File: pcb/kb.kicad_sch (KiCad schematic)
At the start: 72 parts, among them K1 Gateron_LP_2.0, K10 Gateron_LP_2.0, K11 Gateron_LP_2.0, K12 Gateron_LP_2.0, K13 Gateron_LP_2.0, K14 Gateron_LP_2.0, K15 Gateron_LP_2.0, K16 Gateron_LP_2.0, K17 Gateron_LP_2.0, K18 Gateron_LP_2.0, K19 Gateron_LP_2.0, K2 Gateron_LP_2.0, K20 Gateron_LP_2.0, K21 Gateron_LP_2.0, K22 Gateron_LP_2.0, K23 Gateron_LP_2.0, K24 Gateron_LP_2.0, K25 Gateron_LP_2.0, K26 Gateron_LP_2.0, K27 Gateron_LP_2.0, K28 Gateron_LP_2.0, K29 Gateron_LP_2.0, K3 Gateron_LP_2.0, K30 Gateron_LP_2.0, K31 Gateron_LP_2.0, K32 Gateron_LP_2.0, K33 Gateron_LP_2.0, K34 Gateron_LP_2.0, K35 Gateron_LP_2.0, K36 Gateron_LP_2.0, K37 Gateron_LP_2.0, K38 Gateron_LP_2.0, K39 Gateron_LP_2.0, K4 Gateron_LP_2.0, K40 Gateron_LP_2.0, K41 Gateron_LP_2.0, K42 Gateron_LP_2.0, K43 Gateron_LP_2.0, K44 Gateron_LP_2.0, K45 Gateron_LP_2.0, K46 Gateron_LP_2.0, K47 Gateron_LP_2.0, K48 Gateron_LP_2.0, K49 Gateron_LP_2.0, K5 Gateron_LP_2.0, K50 Gateron_LP_2.0, K51 Gateron_LP_2.0, K52 Gateron_LP_2.0, K53 Gateron_LP_2.0, K54 Gateron_LP_2.0, K55 Gateron_LP_2.0, K56 Gateron_LP_2.0, K57 Gateron_LP_2.0, K58 Gateron_LP_2.0, K59 Gateron_LP_2.0, K6 Gateron_LP_2.0, K60 Gateron_LP_2.0, K61 Gateron_LP_2.0, K62 Gateron_LP_2.0, K63 Gateron_LP_2.0, K64 Gateron_LP_2.0, K7 Gateron_LP_2.0, K8 Gateron_LP_2.0, K9 Gateron_LP_2.0, U1 SuperMini nRF52840

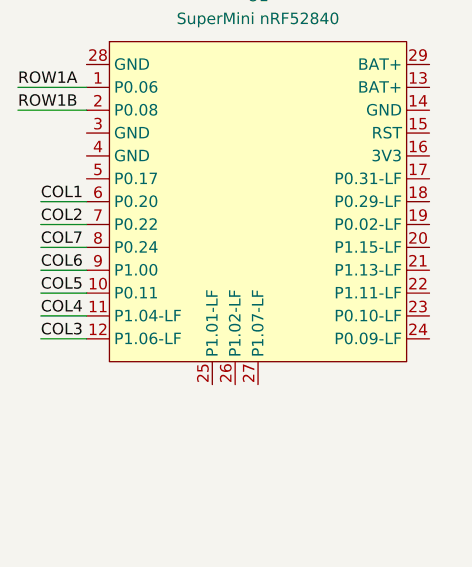
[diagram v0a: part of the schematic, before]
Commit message: routed column traces
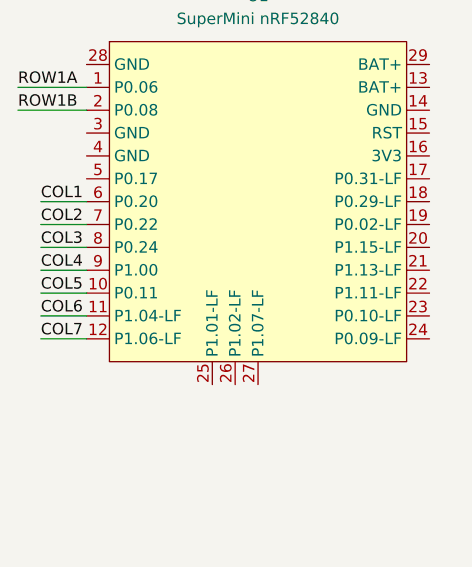
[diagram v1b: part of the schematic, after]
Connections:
- net COL3: now also U1.8 (P0.24); no longer U1.12 (P1.06-LF)
- net COL4: now also U1.9 (P1.00); no longer U1.11 (P1.04-LF)
- net COL6: now also U1.11 (P1.04-LF); no longer U1.9 (P1.00)
- net COL7: now also U1.12 (P1.06-LF); no longer U1.8 (P0.24)

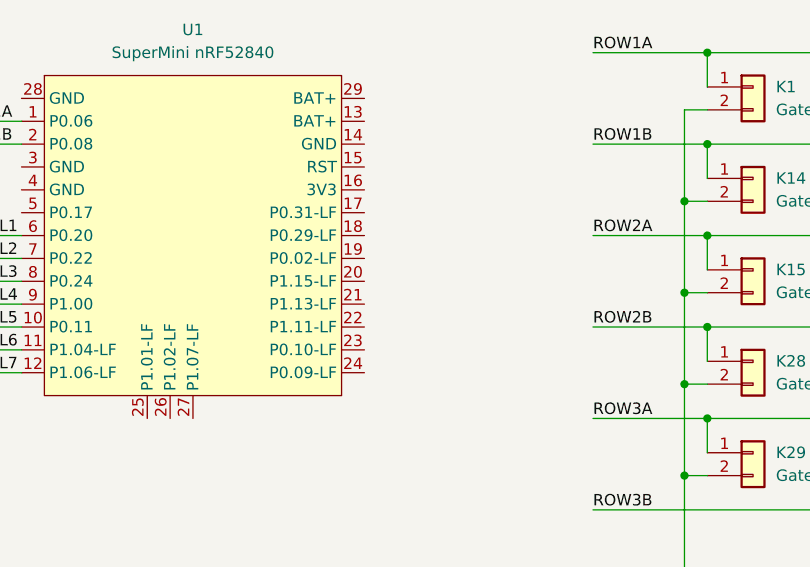
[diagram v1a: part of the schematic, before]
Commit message: routed all traces
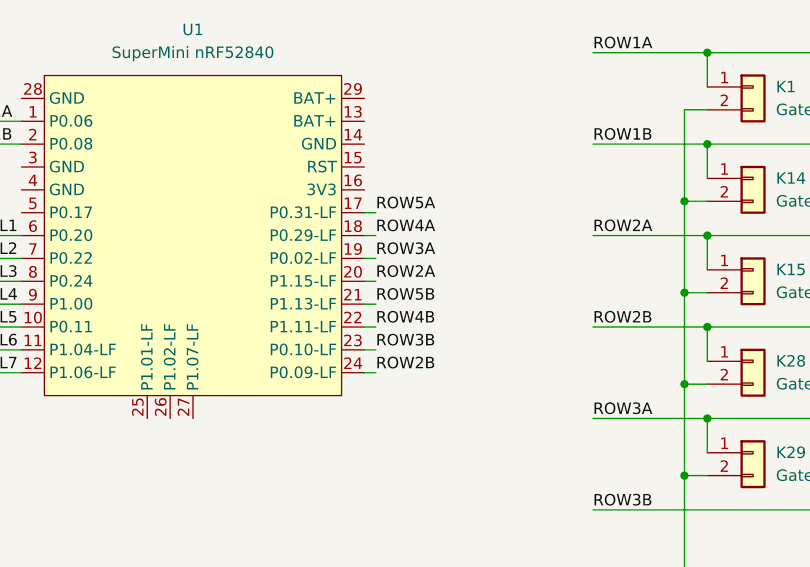
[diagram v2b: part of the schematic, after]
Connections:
- net ROW2A: now also U1.20 (P1.15-LF)
- net ROW2B: now also U1.24 (P0.09-LF)
- net ROW3A: now also U1.19 (P0.02-LF)
- net ROW3B: now also U1.23 (P0.10-LF)
- net ROW4A: now also U1.18 (P0.29-LF)
- net ROW4B: now also U1.22 (P1.11-LF)
- net ROW5A: now also U1.17 (P0.31-LF)
- net ROW5B: now also U1.21 (P1.13-LF)
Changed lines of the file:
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@@
+	(wire
+		(pts
+			(xy 63.5 57.15) (xy 64.77 57.15)
+		)
+		(stroke
+			(width 0)
+			(type default)
+		)
+	)
 	(wire
 		(pts
@@
 	(wire
 		(pts
+			(xy 63.5 44.45) (xy 64.77 44.45)
+		)
+		(stroke
+			(width 0)
+			(type default)
+		)
+	)
+	(wire
+		(pts
 			(xy 175.26 68.58) (xy 177.8 68.58)
 		)
@@
 	(wire
 		(pts
+			(xy 63.5 49.53) (xy 64.77 49.53)
+		)
+		(stroke
+			(width 0)
+			(type default)
+		)
+	)
+	(wire
+		(pts
 			(xy 20.32 41.91) (xy 25.4 41.91)
 		)
@@
 	(wire
 		(pts
+			(xy 63.5 39.37) (xy 64.77 39.37)
+		)
+		(stroke
+			(width 0)
+			(type default)
+		)
+	)
+	(wire
+		(pts
 			(xy 228.6 82.55) (xy 254 82.55)
 		)
@@
 	(wire
 		(pts
+			(xy 63.5 46.99) (xy 64.77 46.99)
+		)
+		(stroke
+			(width 0)
+			(type default)
+		)
+	)
+	(wire
+		(pts
 			(xy 152.4 82.55) (xy 152.4 86.36)
 		)
@@
 	(wire
 		(pts
+			(xy 63.5 54.61) (xy 64.77 54.61)
+		)
+		(stroke
+			(width 0)
+			(type default)
+		)
+	)
+	(wire
+		(pts
 			(xy 152.4 21.59) (xy 152.4 25.4)
 		)
@@
 	(wire
 		(pts
+			(xy 63.5 41.91) (xy 64.77 41.91)
+		)
+		(stroke
+			(width 0)
+			(type default)
+		)
+	)
+	(wire
+		(pts
 			(xy 149.86 88.9) (xy 149.86 99.06)
 		)
@@
 		(pts
 			(xy 200.66 78.74) (xy 203.2 78.74)
+		)
+		(stroke
+			(width 0)
+			(type default)
+		)
+	)
+	(wire
+		(pts
+			(xy 63.5 52.07) (xy 64.77 52.07)
 		)
 		(stroke
@@
 		)
 	)
+	(label "ROW4A"
+		(at 64.77 41.91 0)
+		(effects
+			(font
+				(size 1.27 1.27)
+			)
+			(justify left bottom)
+		)
+	)
+	(label "ROW2A"
+		(at 64.77 46.99 0)
+		(effects
+			(font
+				(size 1.27 1.27)
+			)
+			(justify left bottom)
+		)
+	)
 	(label "COL5"
 		(at 20.32 52.07 0)
@@
 		)
 	)
+	(label "ROW5A"
+		(at 64.77 39.37 0)
+		(effects
+			(font
+				(size 1.27 1.27)
+			)
+			(justify left bottom)
+		)
+	)
 	(label "COL7"
 		(at 251.46 139.7 0)
@@
 		)
 	)
+	(label "ROW4B"
+		(at 64.77 52.07 0)
+		(effects
+			(font
+				(size 1.27 1.27)
+			)
+			(justify left bottom)
+		)
+	)
 	(label "COL2"
 		(at 20.32 44.45 0)
@@
 		)
 	)
+	(label "ROW5B"
+		(at 64.77 49.53 0)
+		(effects
+			(font
+				(size 1.27 1.27)
+			)
+			(justify left bottom)
+		)
+	)
 	(label "COL3"
 		(at 20.32 46.99 0)
@@
 		)
 	)
+	(label "ROW3A"
+		(at 64.77 44.45 0)
+		(effects
+			(font
+				(size 1.27 1.27)
+			)
+			(justify left bottom)
+		)
+	)
 	(label "ROW2A"
 		(at 88.9 41.91 0)
@@
 		)
 	)
+	(label "ROW2B"
+		(at 64.77 57.15 0)
+		(effects
+			(font
+				(size 1.27 1.27)
+			)
+			(justify left bottom)
+		)
+	)
 	(label "COL4"
 		(at 20.32 49.53 0)
@@
 		(effects
 			(font
+				(size 1.27 1.27)
+			)
+			(justify left bottom)
+		)
+	)
+	(label "ROW3B"
+		(at 64.77 54.61 0)
+		(effects
+			(font

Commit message: use smd headers to mitigate switch collision
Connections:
- net COL1: now also U1.5 (P0.17); no longer U1.6 (P0.20)
- net COL2: now also U1.6 (P0.20); no longer U1.7 (P0.22)
- net COL3: now also U1.7 (P0.22); no longer U1.8 (P0.24)
- net COL4: now also U1.8 (P0.24); no longer U1.9 (P1.00)
- net COL5: now also U1.9 (P1.00); no longer U1.10 (P0.11)
- net COL6: now also U1.10 (P0.11); no longer U1.11 (P1.04-LF)
- net COL7: now also U1.11 (P1.04-LF); no longer U1.12 (P1.06-LF)

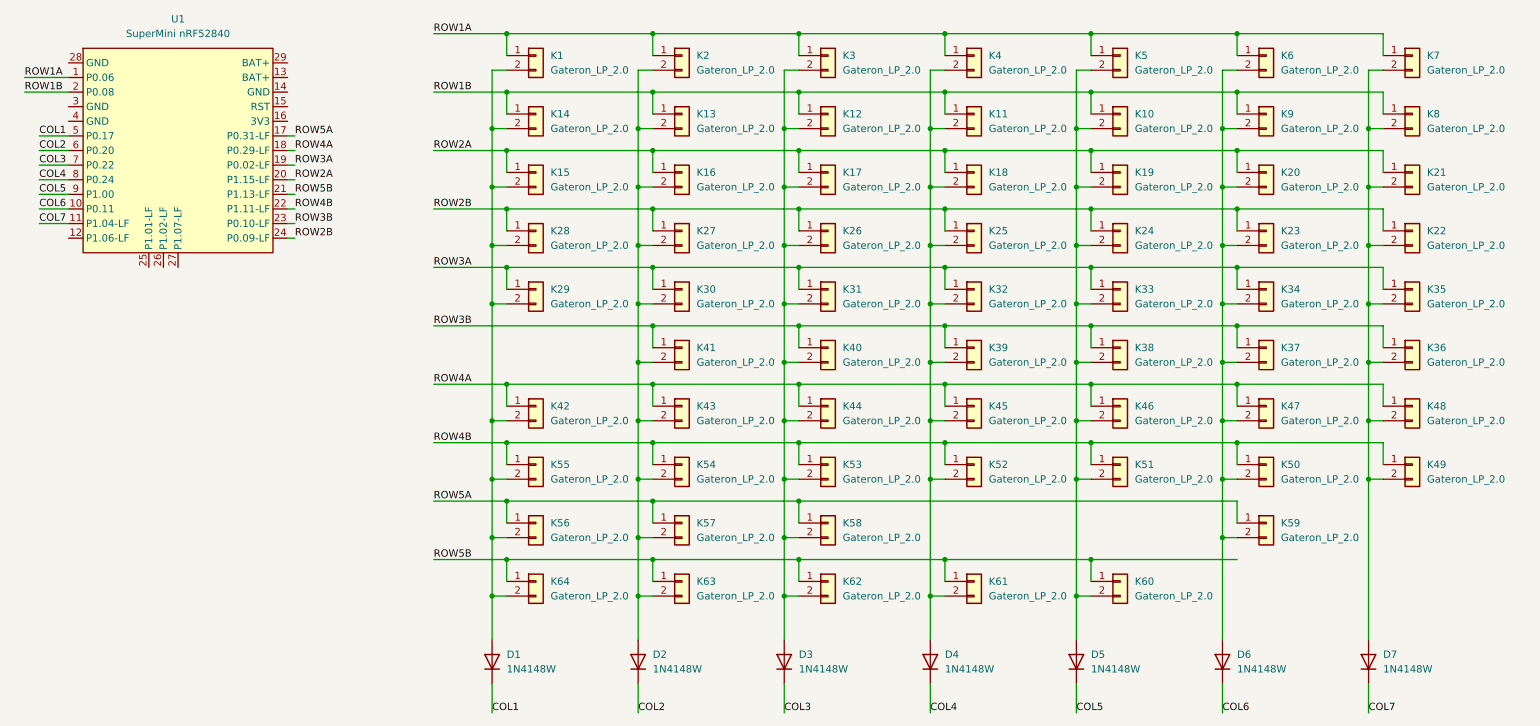
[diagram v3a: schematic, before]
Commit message: change switch reference
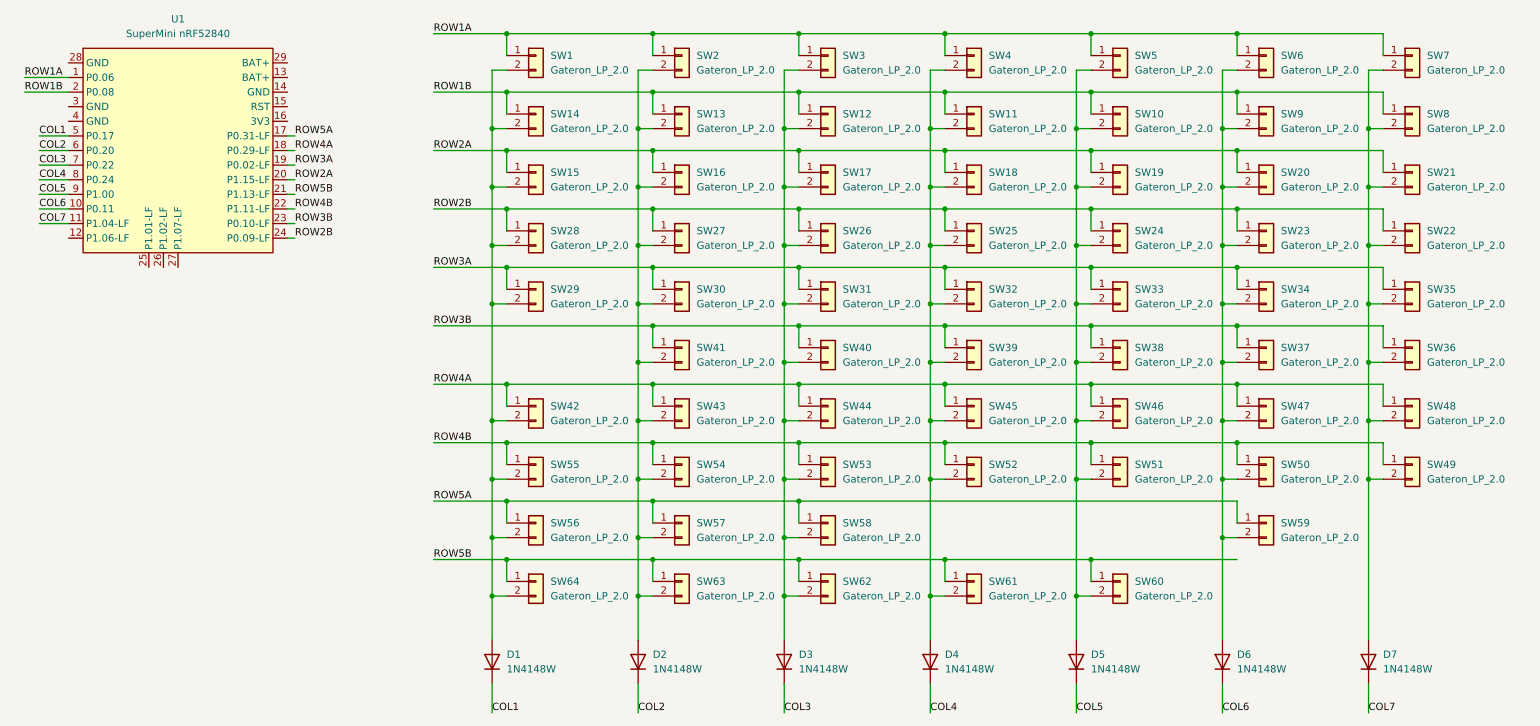
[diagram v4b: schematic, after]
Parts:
- renumbered K1 to SW1, K10 to SW10, K11 to SW11, K12 to SW12, K13 to SW13, K14 to SW14, K15 to SW15, K16 to SW16, K17 to SW17, K18 to SW18, K19 to SW19, K2 to SW2, K20 to SW20, K21 to SW21, K22 to SW22, K23 to SW23, K24 to SW24, K25 to SW25, K26 to SW26, K27 to SW27, K28 to SW28, K29 to SW29, K3 to SW3, K30 to SW30, K31 to SW31, K32 to SW32, K33 to SW33, K34 to SW34, K35 to SW35, K36 to SW36, K37 to SW37, K38 to SW38, K39 to SW39, K4 to SW4, K40 to SW40, K41 to SW41, K42 to SW42, K43 to SW43, K44 to SW44, K45 to SW45, K46 to SW46, K47 to SW47, K48 to SW48, K49 to SW49, K5 to SW5, K50 to SW50, K51 to SW51, K52 to SW52, K53 to SW53, K54 to SW54, K55 to SW55, K56 to SW56, K57 to SW57, K58 to SW58, K59 to SW59, K6 to SW6, K60 to SW60, K61 to SW61, K62 to SW62, K63 to SW63, K64 to SW64, K7 to SW7, K8 to SW8, K9 to SW9

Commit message: rewire and fix everything
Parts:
- added D10, D11, D12, D13, D14, D15, D16, D17, D18, D19, D20, D21, D22, D23, D24, D25, D26, D27, D28, D29, D30, D31, D32, D33, D34, D35, D36, D37, D38, D39, D40, D41, D42, D43, D44, D45, D46, D47, D48, D49, D50, D51, D52, D53, D54, D55, D56, D57, D58, D59, D60, D61, D62, D63, D64, D8, D9: 1N4148W, Diode_SMD:D_SOD-123, symbol Diode:1N4148W
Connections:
- net COL1: now also D14.1 (K); no longer D1.1 (K)
- net COL2: now also D13.1 (K); no longer D2.1 (K)
- net COL3: now also D12.1 (K); no longer D3.1 (K)
- net COL4: now also D11.1 (K); no longer D4.1 (K)
- net COL5: now also D10.1 (K); no longer D5.1 (K)
- net COL6: now also D9.1 (K); no longer D6.1 (K)
- net COL7: now also D8.1 (K); no longer D7.1 (K)
- new net: D56.1 (K), D64.2 (A), SW64.2 (Pin_2)
- new net: D33.1 (K), D46.2 (A), SW46.2 (Pin_2)
- new net: D22.2 (A), D36.1 (K), SW22.2 (Pin_2)
- new net: D32.1 (K), D45.2 (A), SW45.2 (Pin_2)
- new net: D36.2 (A), D49.1 (K), SW36.2 (Pin_2)
- new net: D39.2 (A), D52.1 (K), SW39.2 (Pin_2)
- new net: D21.2 (A), D7.1 (K), SW21.2 (Pin_2)
- new net: D15.1 (K), D29.2 (A), SW29.2 (Pin_2)
- new net: D18.2 (A), D4.1 (K), SW18.2 (Pin_2)
- new net: D4.2 (A), SW4.2 (Pin_2)
- new net: D11.2 (A), D25.1 (K), SW11.2 (Pin_2)
- new net: D19.1 (K), D33.2 (A), SW33.2 (Pin_2)
- new net: D19.2 (A), D5.1 (K), SW19.2 (Pin_2)
- new net: D1.2 (A), SW1.2 (Pin_2)
- new net: D25.2 (A), D39.1 (K), SW25.2 (Pin_2)
- new net: D7.2 (A), SW7.2 (Pin_2)
- new net: D3.2 (A), SW3.2 (Pin_2)
- new net: D22.1 (K), D8.2 (A), SW8.2 (Pin_2)
- new net: D12.2 (A), D26.1 (K), SW12.2 (Pin_2)
- new net: D20.1 (K), D34.2 (A), SW34.2 (Pin_2)
- new net: D20.2 (A), D6.1 (K), SW20.2 (Pin_2)
- new net: D1.1 (K), D15.2 (A), SW15.2 (Pin_2)
- new net: D37.2 (A), D50.1 (K), SW37.2 (Pin_2)
- new net: D50.2 (A), D59.1 (K), SW50.2 (Pin_2)
- new net: D40.2 (A), D53.1 (K), SW40.2 (Pin_2)
- new net: D30.1 (K), D43.2 (A), SW43.2 (Pin_2)
- new net: D52.2 (A), D61.1 (K), SW52.2 (Pin_2)
- new net: D43.1 (K), D57.2 (A), SW57.2 (Pin_2)
- new net: D17.2 (A), D3.1 (K), SW17.2 (Pin_2)
- new net: D51.2 (A), D60.1 (K), SW51.2 (Pin_2)
- new net: D46.1 (K), D60.2 (A), SW60.2 (Pin_2)
- new net: D16.1 (K), D30.2 (A), SW30.2 (Pin_2)
- new net: D23.1 (K), D9.2 (A), SW9.2 (Pin_2)
- new net: D26.2 (A), D40.1 (K), SW26.2 (Pin_2)
- new net: D45.1 (K), D61.2 (A), SW61.2 (Pin_2)
- new net: D14.2 (A), D28.1 (K), SW14.2 (Pin_2)
- new net: D21.1 (K), D35.2 (A), SW35.2 (Pin_2)
- new net: D17.1 (K), D31.2 (A), SW31.2 (Pin_2)
- new net: D18.1 (K), D32.2 (A), SW32.2 (Pin_2)
- new net: D29.1 (K), D42.2 (A), SW42.2 (Pin_2)
- new net: D16.2 (A), D2.1 (K), SW16.2 (Pin_2)
- new net: D48.1 (K), D49.2 (A), SW49.2 (Pin_2)
- new net: D53.2 (A), D62.1 (K), SW53.2 (Pin_2)
- new net: D58.1 (K), D62.2 (A), SW62.2 (Pin_2)
- new net: D23.2 (A), D37.1 (K), SW23.2 (Pin_2)
- new net: D35.1 (K), D48.2 (A), SW48.2 (Pin_2)
- new net: D57.1 (K), D63.2 (A), SW63.2 (Pin_2)
- new net: D27.2 (A), D41.1 (K), SW27.2 (Pin_2)
- new net: D41.2 (A), D54.1 (K), SW41.2 (Pin_2)
- new net: D44.1 (K), D58.2 (A), SW58.2 (Pin_2)
- new net: D31.1 (K), D44.2 (A), SW44.2 (Pin_2)
- new net: D38.2 (A), D51.1 (K), SW38.2 (Pin_2)
- new net: D54.2 (A), D63.1 (K), SW54.2 (Pin_2)
- new net: D5.2 (A), SW5.2 (Pin_2)
- new net: D28.2 (A), D55.1 (K), SW28.2 (Pin_2)
- new net: D42.1 (K), D56.2 (A), SW56.2 (Pin_2)
- new net: D55.2 (A), D64.1 (K), SW55.2 (Pin_2)
- new net: D10.2 (A), D24.1 (K), SW10.2 (Pin_2)
- new net: D24.2 (A), D38.1 (K), SW24.2 (Pin_2)
- new net: D6.2 (A), SW6.2 (Pin_2)
- new net: D13.2 (A), D27.1 (K), SW13.2 (Pin_2)
- new net: D47.1 (K), D59.2 (A), SW59.2 (Pin_2)
- new net: D2.2 (A), SW2.2 (Pin_2)
- new net: D34.1 (K), D47.2 (A), SW47.2 (Pin_2)
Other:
- moved on the sheet: D1, D2, D3, D4, D5, D6, D7, SW10, SW11, SW12, SW13, SW14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

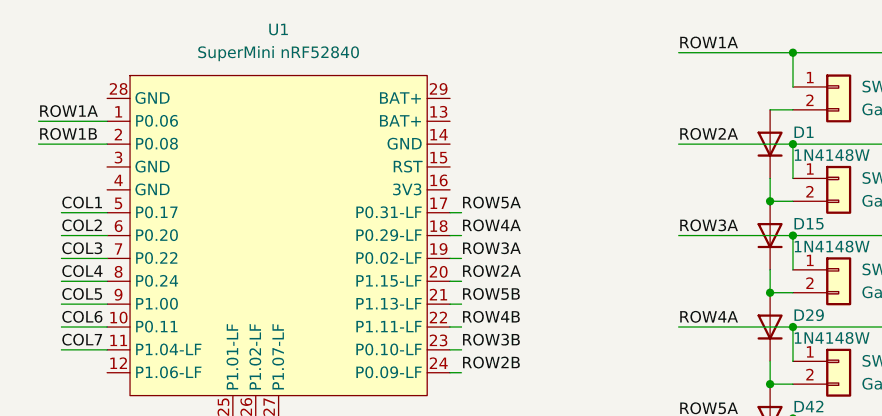
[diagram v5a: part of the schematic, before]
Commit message: shrink 2u hotswap pads
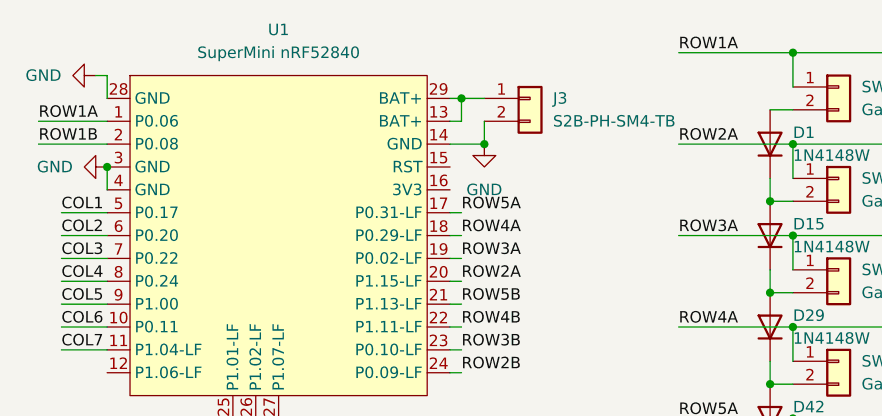
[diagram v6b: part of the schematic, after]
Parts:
- added J3: S2B-PH-SM4-TB, Connector_JST:JST_PH_S2B-PH-SM4-TB_1x02-1MP_P2.00mm_Horizontal, symbol connectors:S2B-PH-SM4-TB
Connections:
- net at U1.13 (BAT+): now also U1.29 (BAT+), J3.1 (Pin_1)
- net GND: now reaches U1.14 (GND)
- net GND: now also U1.28 (GND), U1.3 (GND), U1.4 (GND), J3.2 (Pin_2)

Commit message: checked all tolerances
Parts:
- renumbered J3 to J1
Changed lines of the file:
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@@
 		(dnp no)
 		(fields_autoplaced yes)
-		(property "Reference" "J3"
+		(property "Reference" "J1"
 			(at 74.93 26.6699 0)
 			(effects
@@
 			(project ""
 				(path "/1a8010be-a482-4df4-9d54-41d2f51d2728"
-					(reference "J3")
+					(reference "J1")
 					(unit 1)
 				)

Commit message: battery switch
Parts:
- added SW0: SW_SPDT, Button_Switch_SMD:SW_SPDT_CK_JS102011SAQN, symbol Switch:SW_SPDT
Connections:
- net GND: now also SW0.2 (B); no longer J1.2 (Pin_2)
- new net: J1.2 (Pin_2), SW0.1 (A)
- no-connect marks 0 -> 1
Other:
- moved on the sheet: J1
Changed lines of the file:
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@@
 	)
 	(junction
+		(at 66.04 31.75)
+		(diameter 0)
+		(color 0 0 0 0)
+	)
+	(junction
 		(at 177.8 31.75)
 		(diameter 0)
@@
 	)
 	(junction
-		(at 67.31 31.75)
-		(diameter 0)
-		(color 0 0 0 0)
-	)
-	(junction
 		(at 203.2 31.75)
 		(diameter 0)
@@
 		(color 0 0 0 0)
 	)
+	(no_connect
+		(at 76.2 34.29)
+	)
 	(wire
 		(pts
@@
 	(wire
 		(pts
+			(xy 76.2 26.67) (xy 76.2 29.21)
+		)
+		(stroke
+			(width 0)
+			(type default)
+		)
+	)
+	(wire
+		(pts
 			(xy 99.06 96.52) (xy 99.06 109.22)
 		)
@@
 	(wire
 		(pts
-			(xy 67.31 31.75) (xy 67.31 29.21)
-		)
-		(stroke
-			(width 0)
-			(type default)
-		)
-	)
-	(wire
-		(pts
 			(xy 99.06 27.94) (xy 101.6 27.94)
 		)
@@
 	(wire
 		(pts
+			(xy 64.77 24.13) (xy 64.77 26.67)
+		)
+		(stroke
+			(width 0)
+			(type default)
+		)
+	)
+	(wire
+		(pts
 			(xy 124.46 109.22) (xy 124.46 106.68)
 		)
@@
 	(wire
 		(pts
-			(xy 64.77 26.67) (xy 67.31 26.67)
+			(xy 64.77 24.13) (xy 76.2 24.13)
 		)
 		(stroke
@@
 	(wire
 		(pts
-			(xy 63.5 31.75) (xy 67.31 31.75)
+			(xy 63.5 31.75) (xy 66.04 31.75)
 		)
 		(stroke
@@
 	(symbol
 		(lib_id "connectors:S2B-PH-SM4-TB")
-		(at 72.39 26.67 0)
+		(at 81.28 24.13 0)
 		(unit 1)
 		(exclude_from_sim no)
@@
 		(fields_autoplaced yes)
 		(property "Reference" "J1"
-			(at 74.93 26.6699 0)
+			(at 83.82 24.1299 0)
 			(effects
 				(font
@@
 		)
 		(property "Value" "S2B-PH-SM4-TB"
-			(at 74.93 29.2099 0)
+			(at 83.82 26.6699 0)
 			(effects
 				(font
@@
 		)
 		(property "Footprint" "Connector_JST:JST_PH_S2B-PH-SM4-TB_1x02-1MP_P2.00mm_Horizontal"
-			(at 72.39 26.67 0)
+			(at 81.28 24.13 0)
 			(effects
 				(font
@@
 		)
 		(property "Datasheet" "~"
-			(at 72.39 26.67 0)
+			(at 81.28 24.13 0)
 			(effects
 				(font
@@
 		)
 		(property "Description" "Generic connector, single row, 01x02, script generated (kicad-library-utils/schlib/autogen/connector/)"
-			(at 72.39 26.67 0)
+			(at 81.28 24.13 0)
 			(effects
 				(font
@@
 	(symbol
 		(lib_id "power:GND")
-		(at 67.31 31.75 0)
+		(at 66.04 31.75 0)
 		(unit 1)
 		(exclude_from_sim no)
@@
 		(fields_autoplaced yes)
 		(property "Reference" "#PWR01"
-			(at 67.31 38.1 0)
+			(at 66.04 38.1 0)
 			(effects
 				(font
@@
 		)
 		(property "Value" "GND"
-			(at 67.31 36.83 0)
+			(at 66.04 36.83 0)
 			(effects
 				(font
@@
 		)
 		(property "Footprint" ""
-			(at 67.31 31.75 0)
+			(at 66.04 31.75 0)
 			(effects
 				(font
@@
 		)
 		(property "Datasheet" ""
-			(at 67.31 31.75 0)
+			(at 66.04 31.75 0)
 			(effects
 				(font
@@
 		)
 		(property "Description" "Power symbol creates a global label with name \"GND\" , ground"
-			(at 67.31 31.75 0)
+			(at 66.04 31.75 0)
 			(effects
 				(font
@@
 					(unit 1)
 				)
+			)
+		)
+	)
+	(symbol
+		(lib_id "Switch:SW_SPDT")
+		(at 71.12 31.75 0)
+		(unit 1)
+		(exclude_from_sim no)
+		(in_bom yes)
+		(on_board yes)
+		(dnp no)
+		(fields_autoplaced yes)
+		(property "Reference" "SW0"
+			(at 71.12 22.86 0)
+			(effects
+				(font
+					(size 1.27 1.27)
+				)
+			)
+		)
+		(property "Value" "SW_SPDT"
+			(at 71.12 25.4 0)
+			(effects
+				(font
+					(size 1.27 1.27)
+				)
+			)
+		)
+		(property "Footprint" "Button_Switch_SMD:SW_SPDT_CK_JS102011SAQN"
+			(at 71.12 31.75 0)
+			(effects
+				(font
+					(size 1.27 1.27)
+				)
+				(hide yes)
+			)
+		)
+		(property "Datasheet" "~"
+			(at 71.12 39.37 0)
+			(effects
+				(font
+					(size 1.27 1.27)
+				)
+				(hide yes)
+			)
+		)
+		(property "Description" "Switch, single pole double throw"
+			(at 71.12 31.75 0)
+			(effects
+				(font
+					(size 1.27 1.27)
+				)
+				(hide yes)
+			)
+		)
+		(pin "2"
+		)
+		(pin "1"
+		)
+		(pin "3"
+		)
+		(instances
+			(project ""
+				(path "/1a8010be-a482-4df4-9d54-41d2f51d2728"
+					(reference "SW0")
+					(unit 1)
+				)
